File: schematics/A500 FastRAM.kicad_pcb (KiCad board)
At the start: 2 copper layers, 97.8 x 87.6 mm, 31 parts, among them J1 Microsemi_FlashPro-JTAG-10, U1 68000 Boardside, U10 TPS7333QP, U2 68000 Socket, U3 ATF1502ASV-15JU44, U4 74157, U5 74157, U6 IS41LV16100D, U7 IS41LV16100D, U8 IS41LV16100D, U9 IS41LV16100D

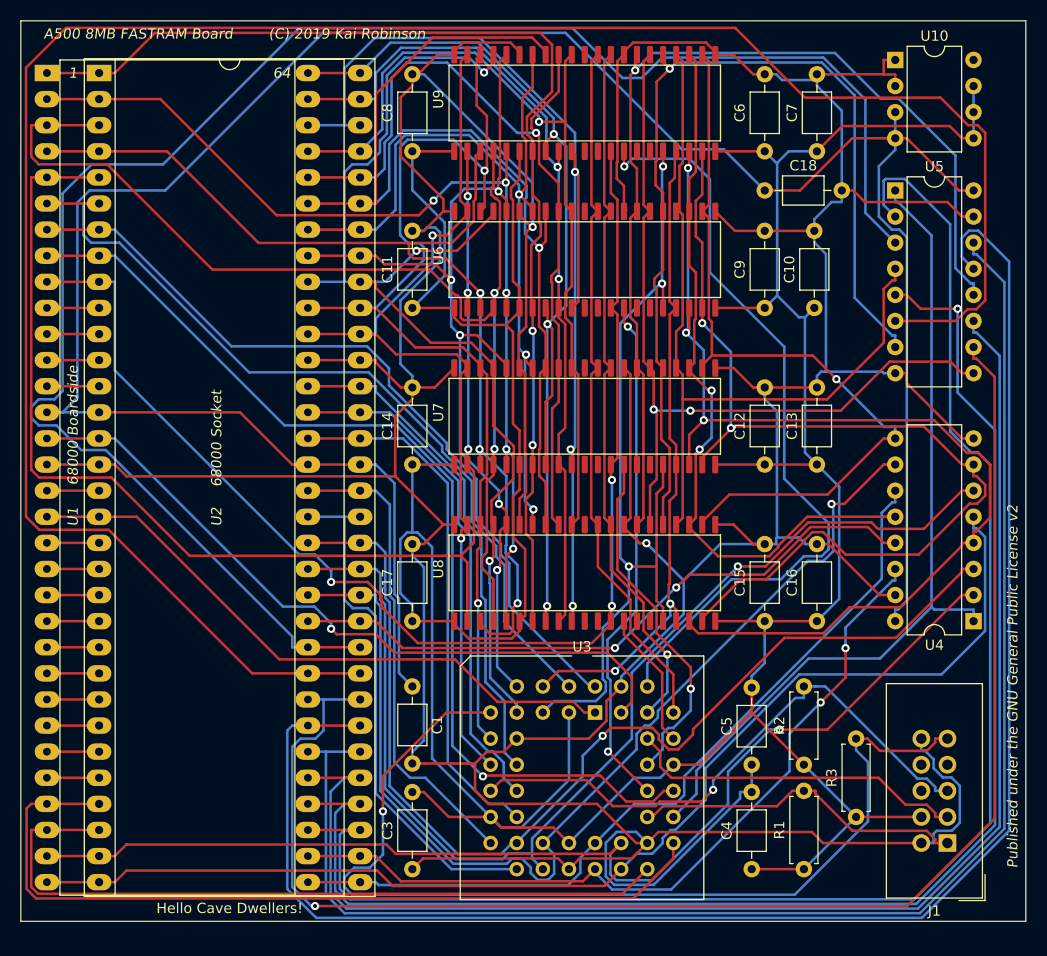
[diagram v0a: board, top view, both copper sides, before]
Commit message: Add files via upload
v1.1 - tweaking layout, compacting things a bit, better routing with less via's
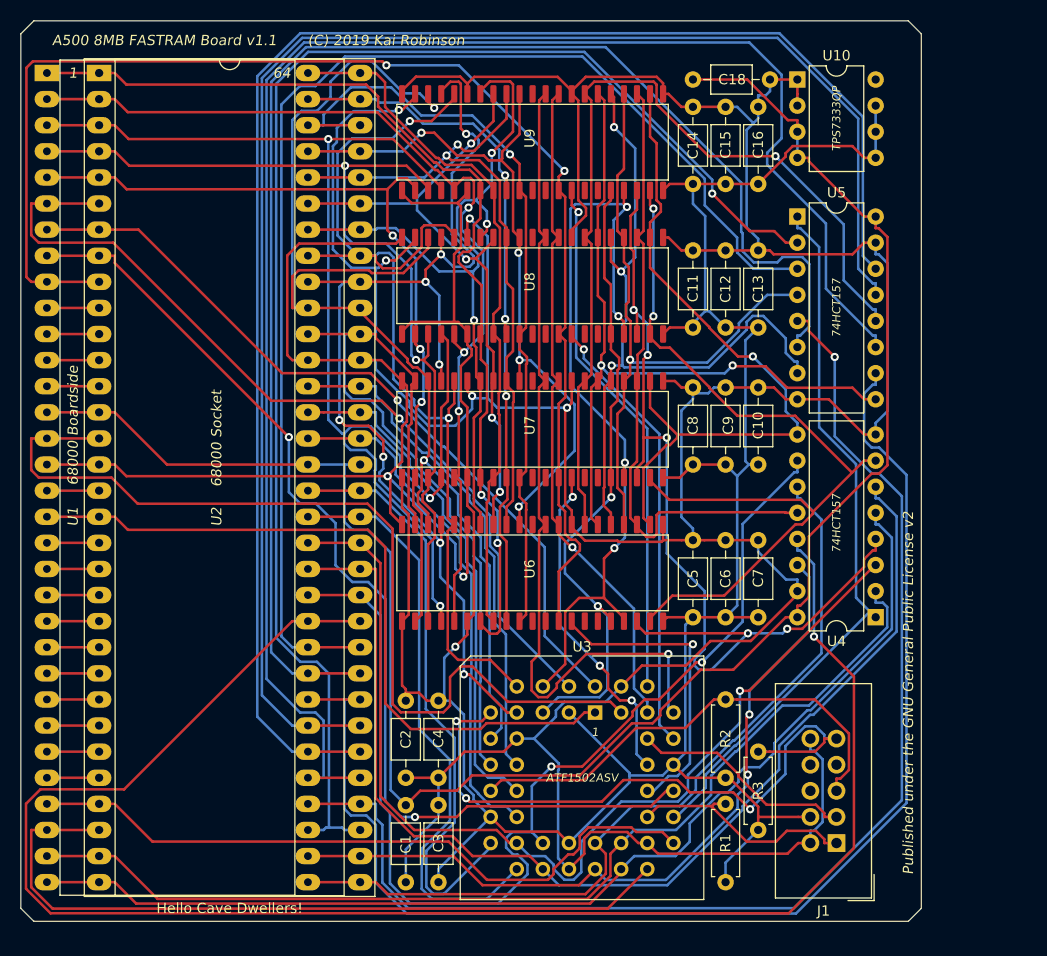
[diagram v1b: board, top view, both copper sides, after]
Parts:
- removed the C11 at (156.2, 58.4)
- added C8: 0.1uF, Capacitor_THT:C_Axial_L3.8mm_D2.6mm_P7.50mm_Horizontal, F.Cu at (183.5, 73.7)
- moved C7 56.5 mm to (189.9, 88.5)
- moved C16 54.2 mm to (189.9, 46.4)
- moved C6 46.2 mm to (186.7, 88.5)
- moved C5 45.9 mm to (183.5, 88.5)
- moved C15 43.5 mm to (186.7, 46.4)
- moved C14 43.1 mm to (183.5, 46.4)
- moved C13 36.2 mm to (189.9, 60.3)
- moved U6 30.9 mm to (166.4, 83.8)
- moved C3 30.5 mm to (158.8, 114.3)
- moved C4 30.5 mm to (158.8, 104.1)
- moved U8 28.4 mm to (166.4, 55.9)
- moved C10 16.2 mm to (189.9, 73.7)
- moved C12 16.0 mm to (186.7, 60.3)
- moved C9 15.7 mm to (186.7, 73.7)
- moved C11 15.1 mm to (183.5, 60.3)
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- renumbered C12 to C11, C13 to C12, C14 to C13, C15 to C14, C16 to C15, C17 to C16, C3 to C2, C4 to C3, C5 to C4, C6 to C5, C7 to C6, C8 to C7
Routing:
- net /CPU_A15: track 63.8 -> 164.9 mm, vias 2 -> 1
- net GND: track 560.6 -> 461.4 mm, vias 2 -> 5
- net /VCC33: track 352.9 -> 284.0 mm, vias 0 -> 1
- net /CPU_A13: track 207.6 -> 140.5 mm
- net VCC: track 235.2 -> 184.6 mm
- net /CPU_A14: track 170.3 -> 122.9 mm
- net /CPU_D0: track 128.7 -> 83.6 mm
- net /CPU_D10: track 99.1 -> 62.7 mm, vias 1 -> 4
- net /TDI: track 99.1 -> 63.8 mm, vias 1 -> 3
- net /DRAM_RAS2: track 13.4 -> 43.5 mm, vias 0 -> 1
- net /CPU_D5: track 96.2 -> 67.9 mm, vias 3 -> 0
- net /CPU_D7: track 103.3 -> 77.1 mm, vias 3 -> 1
- net /CPU_D15: track 91.4 -> 116.9 mm
- net /DRAM_RAS3: track 76.2 -> 51.5 mm
- net /CPU_A9: track 137.8 -> 162.2 mm
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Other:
- board size 97.8 x 87.6 mm -> 87.6 x 87.6 mm
- board text added: "1"
- board text added: "74HCT157"
- board text added: "A500 8MB FASTRAM Board v1.1"
- board text added: "ATF1502ASV"
- board text added: "TPS7333QP"
- board text removed: "A500 8MB FASTRAM Board"

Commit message: Fixing wrong CPU Socket, tweaking layout & routing
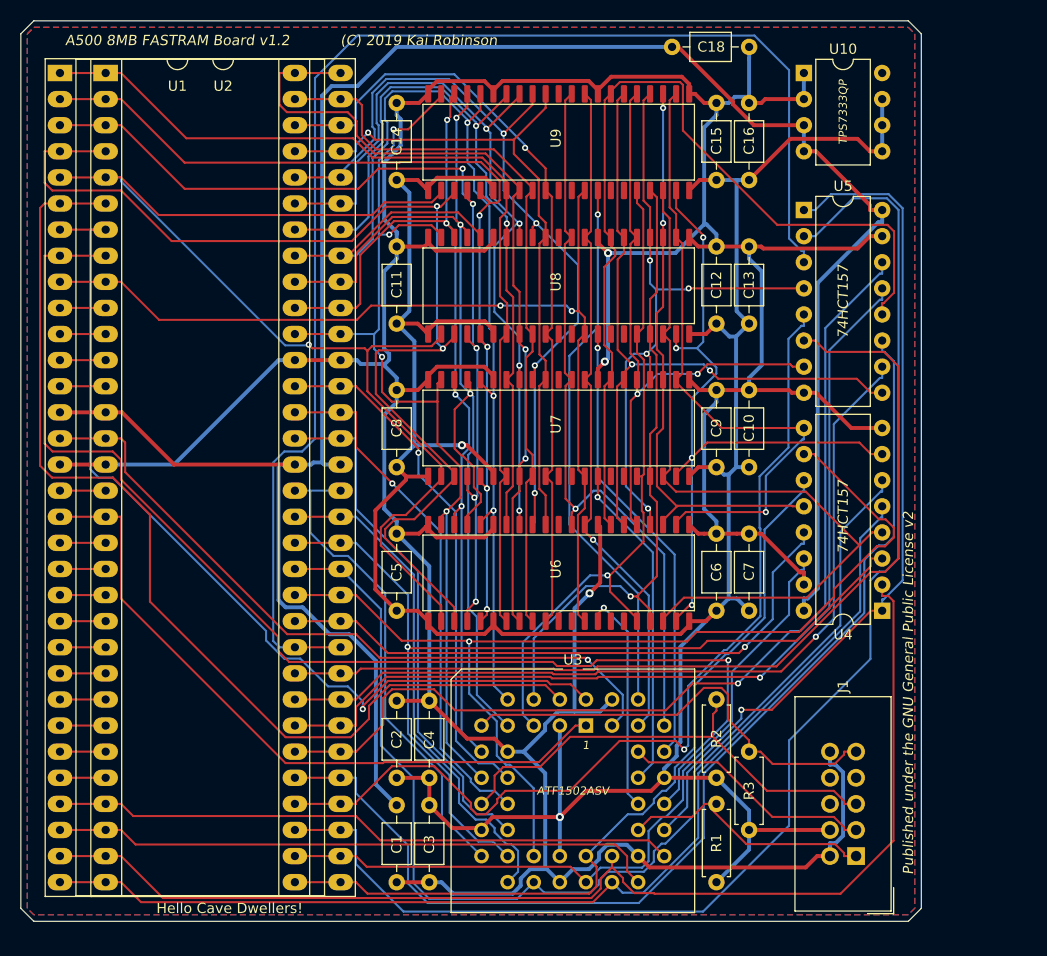
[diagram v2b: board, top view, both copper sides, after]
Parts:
- U1: footprint Package_DIP:DIP-64_W25.4mm_SIL_Headers -> Package_DIP:DIP-64_W22.86mm_Socket_LongPads
- U2: footprint Package_DIP:DIP-64_W25.4mm_Socket_LongPads -> Package_DIP:DIP-64_W22.86mm_Socket_LongPads
- moved U1 39.8 mm to (121.9, 35.6)
- moved C5 28.8 mm to (154.7, 87.9)
- moved C11 28.8 mm to (154.7, 59.9)
- moved C14 28.8 mm to (154.7, 46.0)
- moved C8 28.8 mm to (154.7, 73.9)
- moved C3 7.55 mm to (157.9, 106.8), turned to 270 degrees
- moved C4 7.55 mm to (157.9, 96.6), turned to 270 degrees
- moved C2 7.55 mm to (154.7, 96.6), turned to 270 degrees
- moved C18 3.77 mm to (181.5, 33.0)
- moved U7 2.54 mm to (168.9, 69.7)
- moved U6 2.54 mm to (168.9, 83.8)
- moved U8 2.54 mm to (168.9, 55.9)
- moved U9 2.54 mm to (168.9, 41.9)
- moved J1 2.29 mm to (199.4, 111.8)
- moved U3 1.55 mm to (173.1, 99.1)
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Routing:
- net /CPU_A15: track 164.9 -> 59.0 mm
- net /CPU_A11: track 151.8 -> 91.4 mm, vias 0 -> 1
- net /CPU_A10: track 153.1 -> 96.6 mm, vias 0 -> 1
- net /CPU_A9: track 162.2 -> 107.5 mm
- net /CPU_A13: track 140.5 -> 92.4 mm
- net /CPU_A12: track 128.5 -> 82.4 mm, vias 0 -> 1
- net /CPU_RW: track 131.7 -> 96.3 mm
- net GND: track 461.4 -> 427.6 mm, vias 5 -> 3
- net /CPU_D0: track 83.6 -> 115.3 mm, vias 3 -> 1
- net VCC: track 184.6 -> 214.4 mm
- net /CPU_A8: track 122.4 -> 92.8 mm
- net /CPU_D2: track 122.9 -> 93.4 mm, vias 3 -> 5
- net /CPU_D14: track 121.5 -> 92.7 mm, vias 2 -> 4
- net /CPU_CLK: track 92.2 -> 70.2 mm, vias 0 -> 1
- net /CPU_D15: track 116.9 -> 96.7 mm, vias 2 -> 4
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- added copper zone on B.Cu, net GND
- added copper zone on F.Cu, net GND
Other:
- net class Default: trace_width 0.25 -> 0.2; via_dia 0.8 -> 0.6; via_drill 0.4 -> 0.3
- net class Power added: clearance 0.2, trace_width 0.381, via_dia 0.8, via_drill 0.4
- rule trace_min: 0.2 -> 0.1
- board text added: "A500 8MB FASTRAM Board v1.2"
- board text removed: "A500 8MB FASTRAM Board v1.1"
